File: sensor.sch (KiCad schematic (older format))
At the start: 1 part, among them J1 solder pads

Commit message: changed solder pads to be two separate footprints
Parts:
- removed J1: solder pads, TestPoint:TestPoint_Pad_2.0x2.0mm, symbol Connector:Conn_01x02_Male
- added J19, J20: solder pad, TestPoint:TestPoint_Pad_2.0x2.0mm, symbol Connector:Conn_01x01_Female
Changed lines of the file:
@@
 $Descr A4 11693 8268
 encoding utf-8
-Sheet 3 41
+Sheet 15 41
 Title ""
 Date ""
@@
 Comment4 ""
 $EndDescr
-Text Notes 3700 3050 0    50   ~ 0
+Text HLabel 4750 3550 2    50   Input ~ 0
+Vsense
+Text Notes 3900 3050 0    50   ~ 0
 Note: Strain Gauge connected\nacross screw terminals
-Text HLabel 5400 3500 2    50   Input ~ 0
-Vsense
-Text Notes 3700 3050 0    50   ~ 0
-Note: Strain Gauge connected\nacross screw terminals
-Text HLabel 5400 3500 2    50   Input ~ 0
-Vsense
-$Comp
-L Connector:Conn_01x02_Male J1
-U 1 1 60194E45
-P 5200 3500
-AR Path="/6017CC5E/60194350/60194E45" Ref="J1"  Part="1"
-AR Path="/6017CC5E/6019B999/60194E45" Ref="J2"  Part="1"
-AR Path="/6017CC5E/6019BDB6/60194E45" Ref="J3"  Part="1"
-AR Path="/601927EB/601A1EA6/60194E45" Ref="J4"  Part="1"
-AR Path="/601927EB/601A1EAB/60194E45" Ref="J5"  Part="1"
-AR Path="/601927EB/601A1EB0/60194E45" Ref="J6"  Part="1"
-AR Path="/601B4C0E/60194350/60194E45" Ref="J13"  Part="1"
-AR Path="/601B4C0E/6019B999/60194E45" Ref="J14"  Part="1"
-AR Path="/601B4C0E/6019BDB6/60194E45" Ref="J15"  Part="1"
-AR Path="/601B4C11/601A1EA6/60194E45" Ref="J16"  Part="1"
-AR Path="/601B4C11/601A1EAB/60194E45" Ref="J17"  Part="1"
-AR Path="/601B4C11/601A1EB0/60194E45" Ref="J18"  Part="1"
-AR Path="/601B73B7/60194350/60194E45" Ref="J25"  Part="1"
-AR Path="/601B73B7/6019B999/60194E45" Ref="J26"  Part="1"
-AR Path="/601B73B7/6019BDB6/60194E45" Ref="J27"  Part="1"
-AR Path="/601B73BA/601A1EA6/60194E45" Ref="J28"  Part="1"
-AR Path="/601B73BA/601A1EAB/60194E45" Ref="J29"  Part="1"
-AR Path="/601B73BA/601A1EB0/60194E45" Ref="J30"  Part="1"
-AR Path="/6019C043/601A47AA/60194E45" Ref="J7"  Part="1"
-AR Path="/6019C043/601A47AF/60194E45" Ref="J8"  Part="1"
-AR Path="/6019C043/601A47B4/60194E45" Ref="J9"  Part="1"
-AR Path="/601B4C16/601A47AA/60194E45" Ref="J19"  Part="1"
-AR Path="/601B4C16/601A47AF/60194E45" Ref="J20"  Part="1"
-AR Path="/601B4C16/601A47B4/60194E45" Ref="J21"  Part="1"
-AR Path="/6019DBCE/601A6FCC/60194E45" Ref="J10"  Part="1"
-AR Path="/6019DBCE/601A6FD1/60194E45" Ref="J11"  Part="1"
-AR Path="/6019DBCE/601A6FD6/60194E45" Ref="J12"  Part="1"
-AR Path="/601B4C19/601A6FCC/60194E45" Ref="J22"  Part="1"
-AR Path="/601B4C19/601A6FD1/60194E45" Ref="J23"  Part="1"
-AR Path="/601B4C19/601A6FD6/60194E45" Ref="J24"  Part="1"
-F 0 "J1" H 5000 3500 50  0000 C CNN
-F 1 "solder pads" H 4950 3400 50  0000 C CNN
-F 2 "TestPoint:TestPoint_Pad_2.0x2.0mm" H 5200 3500 50  0001 C CNN
-F 3 "~" H 5200 3500 50  0001 C CNN
-	1    5200 3500
-	1    0    0    -1
-$EndComp
-Text Notes 3700 3050 0    50   ~ 0
-Note: Strain Gauge connected\nacross screw terminals
-Text HLabel 5400 3500 2    50   Input ~ 0
-Vsense
 $Comp
 L power:GND #PWR?
 U 1 1 60194B46
-P 5400 3600
+P 4750 3900
 AR Path="/60132BC3/6013AE22/60194B46" Ref="#PWR?"  Part="1"
 AR Path="/6017CC5E/60194B46" Ref="#PWR?"  Part="1"
@@
 AR Path="/601B4C19/601A6FD1/60194B46" Ref="#PWR074"  Part="1"
 AR Path="/601B4C19/601A6FD6/60194B46" Ref="#PWR075"  Part="1"
-F 0 "#PWR093" H 5400 3350 50  0001 C CNN
-F 1 "GND" H 5405 3427 50  0000 C CNN
-F 2 "" H 5400 3600 50  0001 C CNN
-F 3 "" H 5400 3600 50  0001 C CNN
-	1    5400 3600
+F 0 "#PWR039" H 4750 3650 50  0001 C CNN
+F 1 "GND" H 4755 3727 50  0000 C CNN
+F 2 "" H 4750 3900 50  0001 C CNN
+F 3 "" H 4750 3900 50  0001 C CNN
+	1    4750 3900
 	1    0    0    -1
 $EndComp
+$Comp
+L Connector:Conn_01x01_Female J19
+U 1 1 60B24ECC
+P 4550 3550
+AR Path="/6019DBCE/601A6FCC/60B24ECC" Ref="J19"  Part="1"
+AR Path="/6017CC5E/60194350/60B24ECC" Ref="J1"  Part="1"
+AR Path="/6017CC5E/6019B999/60B24ECC" Ref="J3"  Part="1"
+AR Path="/6017CC5E/6019BDB6/60B24ECC" Ref="J5"  Part="1"
+AR Path="/601927EB/601A1EA6/60B24ECC" Ref="J7"  Part="1"
+AR Path="/601927EB/601A1EAB/60B24ECC" Ref="J9"  Part="1"
+AR Path="/601927EB/601A1EB0/60B24ECC" Ref="J11"  Part="1"
+AR Path="/6019C043/601A47AA/60B24ECC" Ref="J13"  Part="1"
+AR Path="/6019C043/601A47AF/60B24ECC" Ref="J15"  Part="1"
+AR Path="/6019C043/601A47B4/60B24ECC" Ref="J17"  Part="1"
+AR Path="/6019DBCE/601A6FD1/60B24ECC" Ref="J21"  Part="1"
+AR Path="/6019DBCE/601A6FD6/60B24ECC" Ref="J23"  Part="1"
+AR Path="/601B4C0E/60194350/60B24ECC" Ref="J25"  Part="1"
+AR Path="/601B4C0E/6019B999/60B24ECC" Ref="J27"  Part="1"
+AR Path="/601B4C0E/6019BDB6/60B24ECC" Ref="J29"  Part="1"
+AR Path="/601B4C11/601A1EA6/60B24ECC" Ref="J31"  Part="1"
+AR Path="/601B4C11/601A1EAB/60B24ECC" Ref="J33"  Part="1"
+AR Path="/601B4C11/601A1EB0/60B24ECC" Ref="J35"  Part="1"
+AR Path="/601B4C16/601A47AA/60B24ECC" Ref="J37"  Part="1"
+AR Path="/601B4C16/601A47AF/60B24ECC" Ref="J39"  Part="1"
+AR Path="/601B4C16/601A47B4/60B24ECC" Ref="J41"  Part="1"
+AR Path="/601B4C19/601A6FCC/60B24ECC" Ref="J43"  Part="1"
+AR Path="/601B4C19/601A6FD1/60B24ECC" Ref="J45"  Part="1"
+AR Path="/601B4C19/601A6FD6/60B24ECC" Ref="J47"  Part="1"
+AR Path="/601B73B7/60194350/60B24ECC" Ref="J49"  Part="1"
+AR Path="/601B73B7/6019B999/60B24ECC" Ref="J51"  Part="1"
+AR Path="/601B73B7/6019BDB6/60B24ECC" Ref="J53"  Part="1"
+AR Path="/601B73BA/601A1EA6/60B24ECC" Ref="J55"  Part="1"
+AR Path="/601B73BA/601A1EAB/60B24ECC" Ref="J57"  Part="1"
+AR Path="/601B73BA/601A1EB0/60B24ECC" Ref="J59"  Part="1"
+F 0 "J19" H 4442 3325 50  0000 C CNN
+F 1 "solder pad" H 4442 3416 50  0000 C CNN
+F 2 "TestPoint:TestPoint_Pad_2.0x2.0mm" H 4550 3550 50  0001 C CNN
+F 3 "~" H 4550 3550 50  0001 C CNN
+	1    4550 3550
+	-1   0    0    1
+$EndComp
+$Comp
+L Connector:Conn_01x01_Female J20
+U 1 1 60B24F9B
+P 4550 3900
+AR Path="/6019DBCE/601A6FCC/60B24F9B" Ref="J20"  Part="1"
+AR Path="/6017CC5E/60194350/60B24F9B" Ref="J2"  Part="1"
+AR Path="/6017CC5E/6019B999/60B24F9B" Ref="J4"  Part="1"
+AR Path="/6017CC5E/6019BDB6/60B24F9B" Ref="J6"  Part="1"
+AR Path="/601927EB/601A1EA6/60B24F9B" Ref="J8"  Part="1"
+AR Path="/601927EB/601A1EAB/60B24F9B" Ref="J10"  Part="1"
+AR Path="/601927EB/601A1EB0/60B24F9B" Ref="J12"  Part="1"
+AR Path="/6019C043/601A47AA/60B24F9B" Ref="J14"  Part="1"
+AR Path="/6019C043/601A47AF/60B24F9B" Ref="J16"  Part="1"
+AR Path="/6019C043/601A47B4/60B24F9B" Ref="J18"  Part="1"
+AR Path="/6019DBCE/601A6FD1/60B24F9B" Ref="J22"  Part="1"
+AR Path="/6019DBCE/601A6FD6/60B24F9B" Ref="J24"  Part="1"
+AR Path="/601B4C0E/60194350/60B24F9B" Ref="J26"  Part="1"
+AR Path="/601B4C0E/6019B999/60B24F9B" Ref="J28"  Part="1"
+AR Path="/601B4C0E/6019BDB6/60B24F9B" Ref="J30"  Part="1"
+AR Path="/601B4C11/601A1EA6/60B24F9B" Ref="J32"  Part="1"
+AR Path="/601B4C11/601A1EAB/60B24F9B" Ref="J34"  Part="1"
+AR Path="/601B4C11/601A1EB0/60B24F9B" Ref="J36"  Part="1"
+AR Path="/601B4C16/601A47AA/60B24F9B" Ref="J38"  Part="1"
+AR Path="/601B4C16/601A47AF/60B24F9B" Ref="J40"  Part="1"
+AR Path="/601B4C16/601A47B4/60B24F9B" Ref="J42"  Part="1"
+AR Path="/601B4C19/601A6FCC/60B24F9B" Ref="J44"  Part="1"
+AR Path="/601B4C19/601A6FD1/60B24F9B" Ref="J46"  Part="1"
+AR Path="/601B4C19/601A6FD6/60B24F9B" Ref="J48"  Part="1"
+AR Path="/601B73B7/60194350/60B24F9B" Ref="J50"  Part="1"
+AR Path="/601B73B7/6019B999/60B24F9B" Ref="J52"  Part="1"
+AR Path="/601B73B7/6019BDB6/60B24F9B" Ref="J54"  Part="1"
+AR Path="/601B73BA/601A1EA6/60B24F9B" Ref="J56"  Part="1"
+AR Path="/601B73BA/601A1EAB/60B24F9B" Ref="J58"  Part="1"
+AR Path="/601B73BA/601A1EB0/60B24F9B" Ref="J60"  Part="1"
+F 0 "J20" H 4442 3675 50  0000 C CNN
+F 1 "solder pad" H 4442 3766 50  0000 C CNN
+F 2 "TestPoint:TestPoint_Pad_2.0x2.0mm" H 4550 3900 50  0001 C CNN
+F 3 "~" H 4550 3900 50  0001 C CNN
+	1    4550 3900
+	-1   0    0    1
+$EndComp
 $EndSCHEMATC

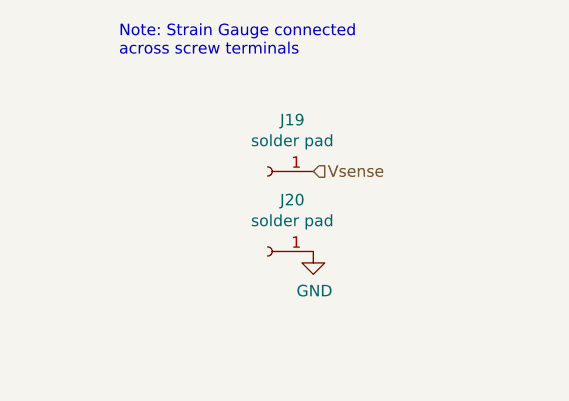
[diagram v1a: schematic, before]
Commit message: switched over remaining rs to 0805
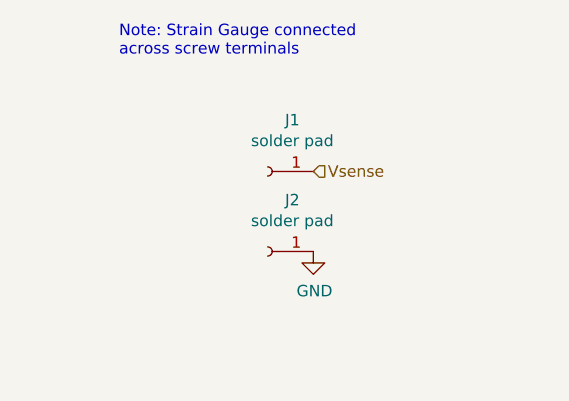
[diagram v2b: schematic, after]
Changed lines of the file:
@@
 $Descr A4 11693 8268
 encoding utf-8
-Sheet 15 41
+Sheet 3 41
 Title ""
 Date ""
@@
 AR Path="/601B4C19/601A6FD1/60194B46" Ref="#PWR074"  Part="1"
 AR Path="/601B4C19/601A6FD6/60194B46" Ref="#PWR075"  Part="1"
-F 0 "#PWR039" H 4750 3650 50  0001 C CNN
+F 0 "#PWR016" H 4750 3650 50  0001 C CNN
 F 1 "GND" H 4755 3727 50  0000 C CNN
 F 2 "" H 4750 3900 50  0001 C CNN
@@
 AR Path="/601B73BA/601A1EAB/60B24ECC" Ref="J57"  Part="1"
 AR Path="/601B73BA/601A1EB0/60B24ECC" Ref="J59"  Part="1"
-F 0 "J19" H 4442 3325 50  0000 C CNN
+F 0 "J1" H 4442 3325 50  0000 C CNN
 F 1 "solder pad" H 4442 3416 50  0000 C CNN
 F 2 "TestPoint:TestPoint_Pad_2.0x2.0mm" H 4550 3550 50  0001 C CNN
@@
 AR Path="/601B73BA/601A1EAB/60B24F9B" Ref="J58"  Part="1"
 AR Path="/601B73BA/601A1EB0/60B24F9B" Ref="J60"  Part="1"
-F 0 "J20" H 4442 3675 50  0000 C CNN
+F 0 "J2" H 4442 3675 50  0000 C CNN
 F 1 "solder pad" H 4442 3766 50  0000 C CNN
 F 2 "TestPoint:TestPoint_Pad_2.0x2.0mm" H 4550 3900 50  0001 C CNN

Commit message: reverted back to screw terminals
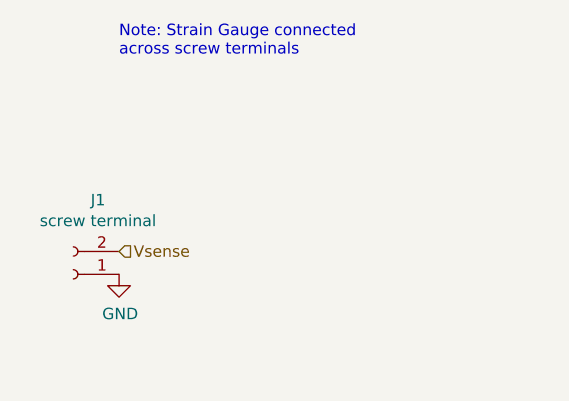
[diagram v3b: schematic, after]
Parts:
- removed J19, J20: solder pad, TestPoint:TestPoint_Pad_2.0x2.0mm, symbol Connector:Conn_01x01_Female
- added J1: screw terminal, Connector_PinHeader_2.54mm:PinHeader_1x02_P2.54mm_Vertical, symbol Connector:Conn_01x02_Female
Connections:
- net GND: now also J1.1 (Pin_1)
- net Vsense: now also J1.2 (Pin_2)
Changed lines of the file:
@@
 Comment4 ""
 $EndDescr
-Text HLabel 4750 3550 2    50   Input ~ 0
+Text HLabel 3900 3900 2    50   Input ~ 0
 Vsense
 Text Notes 3900 3050 0    50   ~ 0
@@
 L power:GND #PWR?
 U 1 1 60194B46
-P 4750 3900
+P 3900 4000
 AR Path="/60132BC3/6013AE22/60194B46" Ref="#PWR?"  Part="1"
 AR Path="/6017CC5E/60194B46" Ref="#PWR?"  Part="1"
@@
 AR Path="/601B4C19/601A6FD1/60194B46" Ref="#PWR074"  Part="1"
 AR Path="/601B4C19/601A6FD6/60194B46" Ref="#PWR075"  Part="1"
-F 0 "#PWR016" H 4750 3650 50  0001 C CNN
-F 1 "GND" H 4755 3727 50  0000 C CNN
-F 2 "" H 4750 3900 50  0001 C CNN
-F 3 "" H 4750 3900 50  0001 C CNN
-	1    4750 3900
+F 0 "#PWR093" H 3900 3750 50  0001 C CNN
+F 1 "GND" H 3905 3827 50  0000 C CNN
+F 2 "" H 3900 4000 50  0001 C CNN
+F 3 "" H 3900 4000 50  0001 C CNN
+	1    3900 4000
 	1    0    0    -1
 $EndComp
 $Comp
-L Connector:Conn_01x01_Female J19
-U 1 1 60B24ECC
-P 4550 3550
-AR Path="/6019DBCE/601A6FCC/60B24ECC" Ref="J19"  Part="1"
-AR Path="/6017CC5E/60194350/60B24ECC" Ref="J1"  Part="1"
-AR Path="/6017CC5E/6019B999/60B24ECC" Ref="J3"  Part="1"
-AR Path="/6017CC5E/6019BDB6/60B24ECC" Ref="J5"  Part="1"
-AR Path="/601927EB/601A1EA6/60B24ECC" Ref="J7"  Part="1"
-AR Path="/601927EB/601A1EAB/60B24ECC" Ref="J9"  Part="1"
-AR Path="/601927EB/601A1EB0/60B24ECC" Ref="J11"  Part="1"
-AR Path="/6019C043/601A47AA/60B24ECC" Ref="J13"  Part="1"
-AR Path="/6019C043/601A47AF/60B24ECC" Ref="J15"  Part="1"
-AR Path="/6019C043/601A47B4/60B24ECC" Ref="J17"  Part="1"
-AR Path="/6019DBCE/601A6FD1/60B24ECC" Ref="J21"  Part="1"
-AR Path="/6019DBCE/601A6FD6/60B24ECC" Ref="J23"  Part="1"
-AR Path="/601B4C0E/60194350/60B24ECC" Ref="J25"  Part="1"
-AR Path="/601B4C0E/6019B999/60B24ECC" Ref="J27"  Part="1"
-AR Path="/601B4C0E/6019BDB6/60B24ECC" Ref="J29"  Part="1"
-AR Path="/601B4C11/601A1EA6/60B24ECC" Ref="J31"  Part="1"
-AR Path="/601B4C11/601A1EAB/60B24ECC" Ref="J33"  Part="1"
-AR Path="/601B4C11/601A1EB0/60B24ECC" Ref="J35"  Part="1"
-AR Path="/601B4C16/601A47AA/60B24ECC" Ref="J37"  Part="1"
-AR Path="/601B4C16/601A47AF/60B24ECC" Ref="J39"  Part="1"
-AR Path="/601B4C16/601A47B4/60B24ECC" Ref="J41"  Part="1"
-AR Path="/601B4C19/601A6FCC/60B24ECC" Ref="J43"  Part="1"
-AR Path="/601B4C19/601A6FD1/60B24ECC" Ref="J45"  Part="1"
-AR Path="/601B4C19/601A6FD6/60B24ECC" Ref="J47"  Part="1"
-AR Path="/601B73B7/60194350/60B24ECC" Ref="J49"  Part="1"
-AR Path="/601B73B7/6019B999/60B24ECC" Ref="J51"  Part="1"
-AR Path="/601B73B7/6019BDB6/60B24ECC" Ref="J53"  Part="1"
-AR Path="/601B73BA/601A1EA6/60B24ECC" Ref="J55"  Part="1"
-AR Path="/601B73BA/601A1EAB/60B24ECC" Ref="J57"  Part="1"
-AR Path="/601B73BA/601A1EB0/60B24ECC" Ref="J59"  Part="1"
-F 0 "J1" H 4442 3325 50  0000 C CNN
-F 1 "solder pad" H 4442 3416 50  0000 C CNN
-F 2 "TestPoint:TestPoint_Pad_2.0x2.0mm" H 4550 3550 50  0001 C CNN
-F 3 "~" H 4550 3550 50  0001 C CNN
-	1    4550 3550
+L Connector:Conn_01x02_Female J1
+U 1 1 60B3291B
+P 3700 4000
+AR Path="/6017CC5E/60194350/60B3291B" Ref="J1"  Part="1"
+AR Path="/6017CC5E/6019B999/60B3291B" Ref="J2"  Part="1"
+AR Path="/6017CC5E/6019BDB6/60B3291B" Ref="J3"  Part="1"
+AR Path="/601927EB/601A1EA6/60B3291B" Ref="J4"  Part="1"
+AR Path="/601927EB/601A1EAB/60B3291B" Ref="J5"  Part="1"
+AR Path="/601927EB/601A1EB0/60B3291B" Ref="J6"  Part="1"
+AR Path="/6019C043/601A47AA/60B3291B" Ref="J7"  Part="1"
+AR Path="/6019C043/601A47AF/60B3291B" Ref="J8"  Part="1"
+AR Path="/6019C043/601A47B4/60B3291B" Ref="J9"  Part="1"
+AR Path="/6019DBCE/601A6FCC/60B3291B" Ref="J10"  Part="1"
+AR Path="/6019DBCE/601A6FD1/60B3291B" Ref="J11"  Part="1"
+AR Path="/6019DBCE/601A6FD6/60B3291B" Ref="J12"  Part="1"
+AR Path="/601B4C0E/60194350/60B3291B" Ref="J13"  Part="1"
+AR Path="/601B4C0E/6019B999/60B3291B" Ref="J14"  Part="1"
+AR Path="/601B4C0E/6019BDB6/60B3291B" Ref="J15"  Part="1"
+AR Path="/601B4C11/601A1EA6/60B3291B" Ref="J16"  Part="1"
+AR Path="/601B4C11/601A1EAB/60B3291B" Ref="J17"  Part="1"
+AR Path="/601B4C11/601A1EB0/60B3291B" Ref="J18"  Part="1"
+AR Path="/601B4C16/601A47AA/60B3291B" Ref="J19"  Part="1"
+AR Path="/601B4C16/601A47AF/60B3291B" Ref="J20"  Part="1"
+AR Path="/601B4C16/601A47B4/60B3291B" Ref="J21"  Part="1"
+AR Path="/601B4C19/601A6FCC/60B3291B" Ref="J22"  Part="1"
+AR Path="/601B4C19/601A6FD1/60B3291B" Ref="J23"  Part="1"
+AR Path="/601B4C19/601A6FD6/60B3291B" Ref="J24"  Part="1"
+AR Path="/601B73B7/60194350/60B3291B" Ref="J25"  Part="1"
+AR Path="/601B73B7/6019B999/60B3291B" Ref="J26"  Part="1"
+AR Path="/601B73B7/6019BDB6/60B3291B" Ref="J27"  Part="1"
+AR Path="/601B73BA/601A1EA6/60B3291B" Ref="J28"  Part="1"
+AR Path="/601B73BA/601A1EAB/60B3291B" Ref="J29"  Part="1"
+AR Path="/601B73BA/601A1EB0/60B3291B" Ref="J30"  Part="1"
+F 0 "J1" H 3592 3675 50  0000 C CNN
+F 1 "screw terminal" H 3592 3766 50  0000 C CNN
+F 2 "Connector_PinHeader_2.54mm:PinHeader_1x02_P2.54mm_Vertical" H 3700 4000 50  0001 C CNN
+F 3 "~" H 3700 4000 50  0001 C CNN
+	1    3700 4000
 	-1   0    0    1
 $EndComp
-$Comp
-L Connector:Conn_01x01_Female J20
-U 1 1 60B24F9B
-P 4550 3900
-AR Path="/6019DBCE/601A6FCC/60B24F9B" Ref="J20"  Part="1"
-AR Path="/6017CC5E/60194350/60B24F9B" Ref="J2"  Part="1"
-AR Path="/6017CC5E/6019B999/60B24F9B" Ref="J4"  Part="1"
-AR Path="/6017CC5E/6019BDB6/60B24F9B" Ref="J6"  Part="1"
-AR Path="/601927EB/601A1EA6/60B24F9B" Ref="J8"  Part="1"
-AR Path="/601927EB/601A1EAB/60B24F9B" Ref="J10"  Part="1"
-AR Path="/601927EB/601A1EB0/60B24F9B" Ref="J12"  Part="1"
-AR Path="/6019C043/601A47AA/60B24F9B" Ref="J14"  Part="1"
-AR Path="/6019C043/601A47AF/60B24F9B" Ref="J16"  Part="1"
-AR Path="/6019C043/601A47B4/60B24F9B" Ref="J18"  Part="1"
-AR Path="/6019DBCE/601A6FD1/60B24F9B" Ref="J22"  Part="1"
-AR Path="/6019DBCE/601A6FD6/60B24F9B" Ref="J24"  Part="1"
-AR Path="/601B4C0E/60194350/60B24F9B" Ref="J26"  Part="1"
-AR Path="/601B4C0E/6019B999/60B24F9B" Ref="J28"  Part="1"
-AR Path="/601B4C0E/6019BDB6/60B24F9B" Ref="J30"  Part="1"
-AR Path="/601B4C11/601A1EA6/60B24F9B" Ref="J32"  Part="1"
-AR Path="/601B4C11/601A1EAB/60B24F9B" Ref="J34"  Part="1"
-AR Path="/601B4C11/601A1EB0/60B24F9B" Ref="J36"  Part="1"
-AR Path="/601B4C16/601A47AA/60B24F9B" Ref="J38"  Part="1"
-AR Path="/601B4C16/601A47AF/60B24F9B" Ref="J40"  Part="1"
-AR Path="/601B4C16/601A47B4/60B24F9B" Ref="J42"  Part="1"
-AR Path="/601B4C19/601A6FCC/60B24F9B" Ref="J44"  Part="1"
-AR Path="/601B4C19/601A6FD1/60B24F9B" Ref="J46"  Part="1"
-AR Path="/601B4C19/601A6FD6/60B24F9B" Ref="J48"  Part="1"
-AR Path="/601B73B7/60194350/60B24F9B" Ref="J50"  Part="1"
-AR Path="/601B73B7/6019B999/60B24F9B" Ref="J52"  Part="1"
-AR Path="/601B73B7/6019BDB6/60B24F9B" Ref="J54"  Part="1"
-AR Path="/601B73BA/601A1EA6/60B24F9B" Ref="J56"  Part="1"
-AR Path="/601B73BA/601A1EAB/60B24F9B" Ref="J58"  Part="1"
-AR Path="/601B73BA/601A1EB0/60B24F9B" Ref="J60"  Part="1"
-F 0 "J2" H 4442 3675 50  0000 C CNN
-F 1 "solder pad" H 4442 3766 50  0000 C CNN
-F 2 "TestPoint:TestPoint_Pad_2.0x2.0mm" H 4550 3900 50  0001 C CNN
-F 3 "~" H 4550 3900 50  0001 C CNN
-	1    4550 3900
-	-1   0    0    1
-$EndComp

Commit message: changed to 1.00mm screw term holes
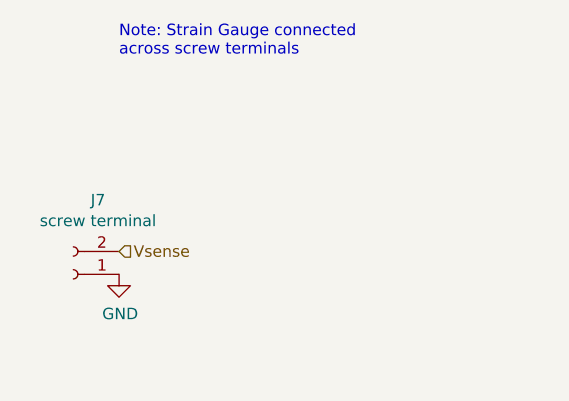
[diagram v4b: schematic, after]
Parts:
- J1: footprint Connector_PinHeader_2.54mm:PinHeader_1x02_P2.54mm_Vertical -> Connector_PinHeader_1.00mm:PinHeader_1x02_P1.00mm_Vertical
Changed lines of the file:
@@
 $Descr A4 11693 8268
 encoding utf-8
-Sheet 3 41
+Sheet 11 41
 Title ""
 Date ""
@@
 AR Path="/601B4C19/601A6FD1/60194B46" Ref="#PWR074"  Part="1"
 AR Path="/601B4C19/601A6FD6/60194B46" Ref="#PWR075"  Part="1"
-F 0 "#PWR093" H 3900 3750 50  0001 C CNN
+F 0 "#PWR032" H 3900 3750 50  0001 C CNN
 F 1 "GND" H 3905 3827 50  0000 C CNN
 F 2 "" H 3900 4000 50  0001 C CNN
@@
 AR Path="/601B73BA/601A1EAB/60B3291B" Ref="J29"  Part="1"
 AR Path="/601B73BA/601A1EB0/60B3291B" Ref="J30"  Part="1"
-F 0 "J1" H 3592 3675 50  0000 C CNN
+F 0 "J7" H 3592 3675 50  0000 C CNN
 F 1 "screw terminal" H 3592 3766 50  0000 C CNN
-F 2 "Connector_PinHeader_2.54mm:PinHeader_1x02_P2.54mm_Vertical" H 3700 4000 50  0001 C CNN
+F 2 "Connector_PinHeader_1.00mm:PinHeader_1x02_P1.00mm_Vertical" H 3700 4000 50  0001 C CNN
 F 3 "~" H 3700 4000 50  0001 C CNN
 	1    3700 4000

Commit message: changed connector verbage
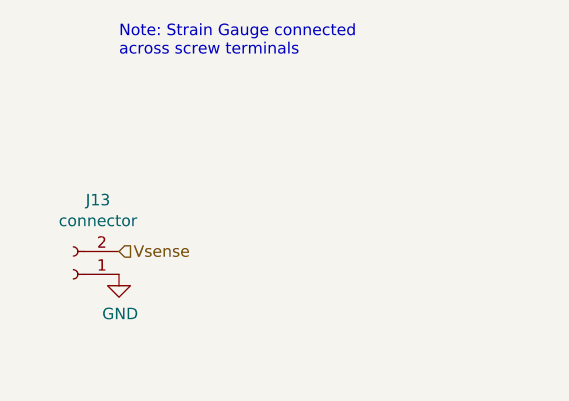
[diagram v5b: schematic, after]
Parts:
- J1: value screw terminal -> connector
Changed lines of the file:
@@
 $Descr A4 11693 8268
 encoding utf-8
-Sheet 11 41
+Sheet 19 41
 Title ""
 Date ""
@@
 AR Path="/601B4C19/601A6FD1/60194B46" Ref="#PWR074"  Part="1"
 AR Path="/601B4C19/601A6FD6/60194B46" Ref="#PWR075"  Part="1"
-F 0 "#PWR032" H 3900 3750 50  0001 C CNN
+F 0 "#PWR050" H 3900 3750 50  0001 C CNN
 F 1 "GND" H 3905 3827 50  0000 C CNN
 F 2 "" H 3900 4000 50  0001 C CNN
@@
 AR Path="/601B73BA/601A1EAB/60B3291B" Ref="J29"  Part="1"
 AR Path="/601B73BA/601A1EB0/60B3291B" Ref="J30"  Part="1"
-F 0 "J7" H 3592 3675 50  0000 C CNN
-F 1 "screw terminal" H 3592 3766 50  0000 C CNN
+F 0 "J13" H 3592 3675 50  0000 C CNN
+F 1 "connector" H 3592 3766 50  0000 C CNN
 F 2 "Connector_PinHeader_1.00mm:PinHeader_1x02_P1.00mm_Vertical" H 3700 4000 50  0001 C CNN
 F 3 "~" H 3700 4000 50  0001 C CNN

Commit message: fixed all drc errors before making new connections
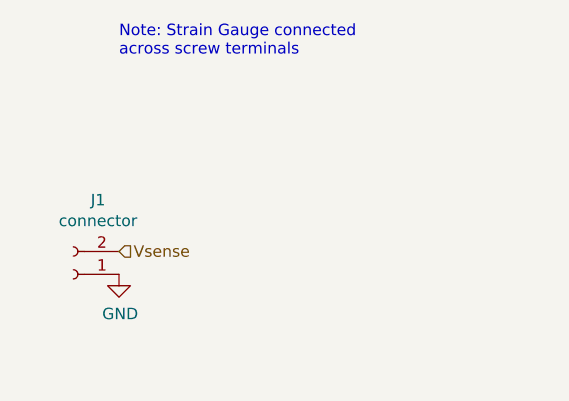
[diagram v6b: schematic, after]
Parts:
- J1: footprint Connector_PinHeader_1.00mm:PinHeader_1x02_P1.00mm_Vertical -> Connector_PinHeader_1.27mm:PinHeader_1x02_P1.27mm_Vertical
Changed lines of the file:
@@
 $Descr A4 11693 8268
 encoding utf-8
-Sheet 19 41
+Sheet 3 41
 Title ""
 Date ""
@@
 AR Path="/601B4C19/601A6FD1/60194B46" Ref="#PWR074"  Part="1"
 AR Path="/601B4C19/601A6FD6/60194B46" Ref="#PWR075"  Part="1"
-F 0 "#PWR050" H 3900 3750 50  0001 C CNN
+F 0 "#PWR016" H 3900 3750 50  0001 C CNN
 F 1 "GND" H 3905 3827 50  0000 C CNN
 F 2 "" H 3900 4000 50  0001 C CNN
@@
 AR Path="/601B73BA/601A1EAB/60B3291B" Ref="J29"  Part="1"
 AR Path="/601B73BA/601A1EB0/60B3291B" Ref="J30"  Part="1"
-F 0 "J13" H 3592 3675 50  0000 C CNN
+F 0 "J1" H 3592 3675 50  0000 C CNN
 F 1 "connector" H 3592 3766 50  0000 C CNN
-F 2 "Connector_PinHeader_1.00mm:PinHeader_1x02_P1.00mm_Vertical" H 3700 4000 50  0001 C CNN
+F 2 "Connector_PinHeader_1.27mm:PinHeader_1x02_P1.27mm_Vertical" H 3700 4000 50  0001 C CNN
 F 3 "~" H 3700 4000 50  0001 C CNN
 	1    3700 4000
